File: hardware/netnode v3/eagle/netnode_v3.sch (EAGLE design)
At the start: 30 parts, among them IC1 TSR-1, IC2 PIC18F4K80, IC3 FOD060L, SW1 431181015816, X1 DC10R, X2 XPORT

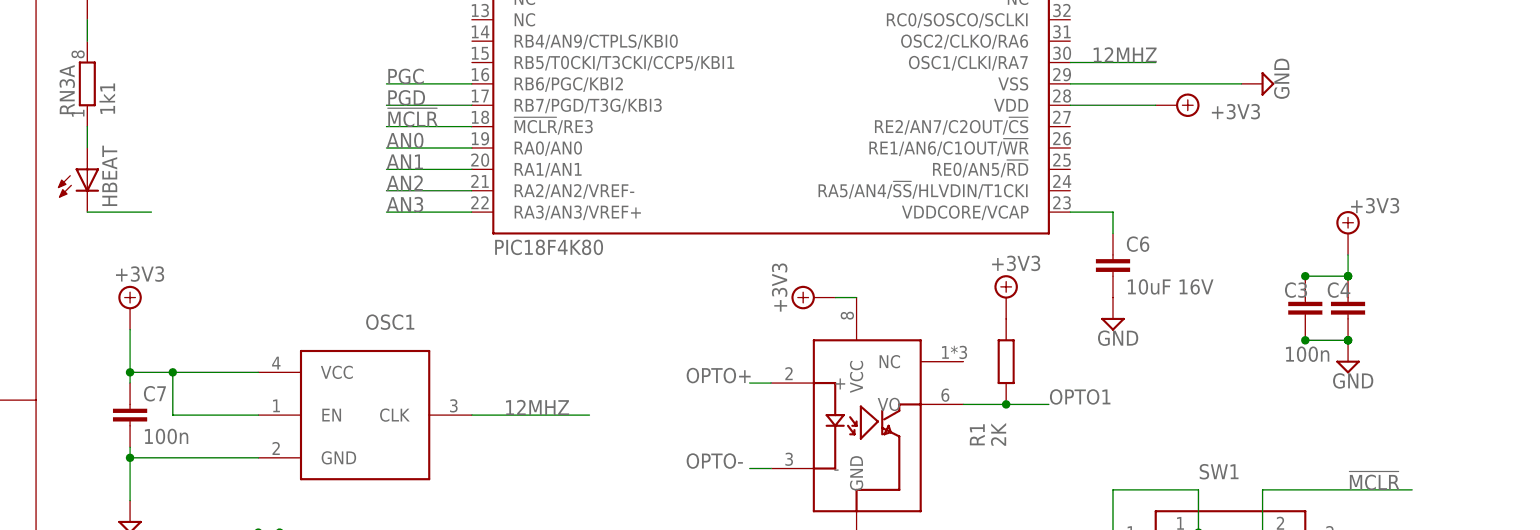
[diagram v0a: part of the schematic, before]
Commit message: Final fixes for boardout.
Added decoupling caps, fixed silkscreen, reviewed compontents
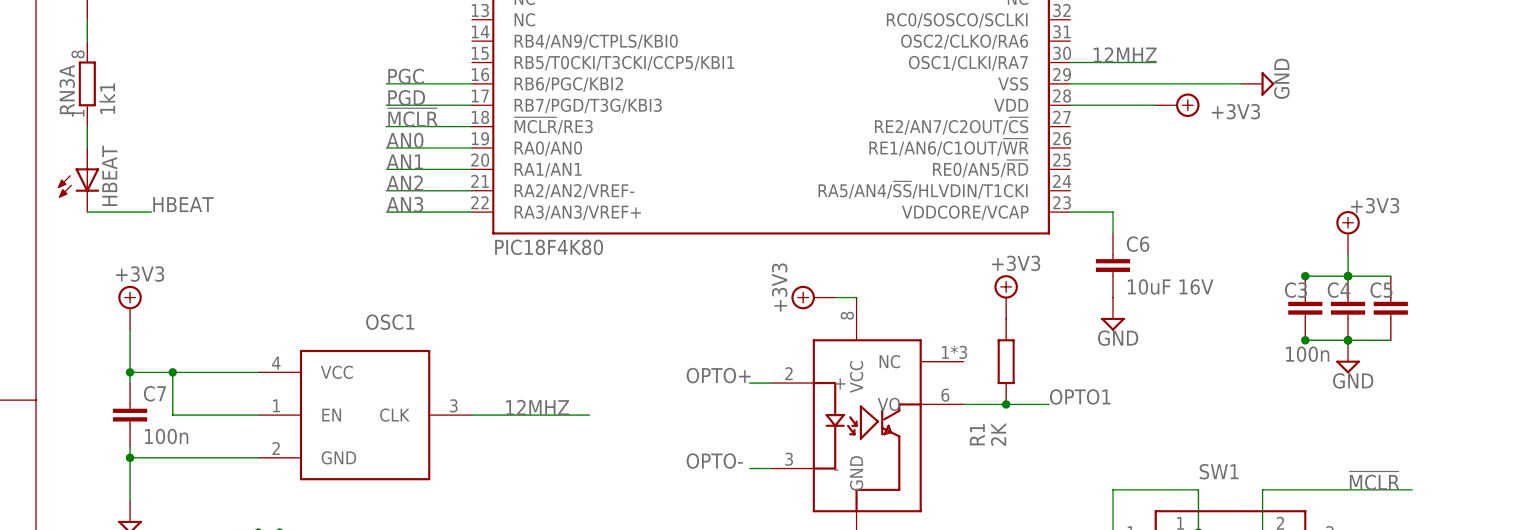
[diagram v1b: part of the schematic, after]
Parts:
- added C5: 100n, rcl:C-EUC0805
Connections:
- net N$11 renamed VDDCAP
- net +3V3: now also C5.1
- net GND: now also C5.2
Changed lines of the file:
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@@
 <?xml version="1.0" encoding="utf-8"?>
 <!DOCTYPE eagle SYSTEM "eagle.dtd">
-<eagle version="6.3">
+<eagle version="6.2">
 <drawing>
 <settings>
@@
 <part name="SW1" library="Eagle_Wuerth_Elektronik_Switch_Power_Elements" deviceset="431181015816" device=""/>
 <part name="V6" library="supply2" deviceset="GND" device=""/>
+<part name="C5" library="rcl" deviceset="C-EU" device="C0805" value="100n">
+<attribute name="MF" value="AVX"/>
+<attribute name="MPN" value="08055C104JAT2A"/>
+<attribute name="OC_FARNELL" value="1740673"/>
+</part>
 </parts>
 <sheets>
@@
 <instance part="SW1" gate="G$1" x="226.06" y="66.04"/>
 <instance part="V6" gate="GND" x="213.36" y="71.12"/>
+<instance part="C5" gate="G$1" x="248.92" y="101.6" smashed="yes">
+<attribute name="NAME" x="246.38" y="101.6" size="1.778" layer="95"/>
+<attribute name="OC_FARNELL" x="248.92" y="101.6" size="1.778" layer="96" rot="R90" display="off"/>
+<attribute name="MF" x="248.92" y="101.6" size="1.778" layer="96" rot="R90" display="off"/>
+<attribute name="MPN" x="248.92" y="101.6" size="1.778" layer="96" rot="R90" display="off"/>
+</instance>
 </instances>
 <busses>
@@
 <pinref part="C3" gate="G$1" pin="2"/>
 <pinref part="C4" gate="G$1" pin="2"/>
+<pinref part="C5" gate="G$1" pin="2"/>
+<wire x1="243.84" y1="96.52" x2="248.92" y2="96.52" width="0.1524" layer="91"/>
 </segment>
 <segment>
@@
 <pinref part="C4" gate="G$1" pin="1"/>
 <pinref part="V15" gate="+3V3" pin="+3V3"/>
+<pinref part="C5" gate="G$1" pin="1"/>
+<wire x1="243.84" y1="104.14" x2="248.92" y2="104.14" width="0.1524" layer="91"/>
 </segment>
 <segment>
@@
 <pinref part="HBEAT" gate="G$1" pin="C"/>
 <wire x1="93.98" y1="111.76" x2="101.6" y2="111.76" width="0.1524" layer="91"/>
+<label x="101.6" y="111.76" size="1.778" layer="95"/>
 </segment>
 <segment>
@@
 </segment>
 </net>
-<net name="N$11" class="0">
+<net name="VDDCAP" class="0">
 <segment>
 <pinref part="IC2" gate="G$1" pin="VDDCORE/VCAP"/>
@@
 </sheet>
 </sheets>
+<errors>
+</errors>
 </schematic>
 </drawing>
